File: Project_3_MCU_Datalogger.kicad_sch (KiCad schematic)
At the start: 25 parts, among them U1 24LC1025, U2 24LC1025, U3 DS1337S_, U4 ATMEGA328P-AU, Y1 16MHz, Y2 32.768 kHz

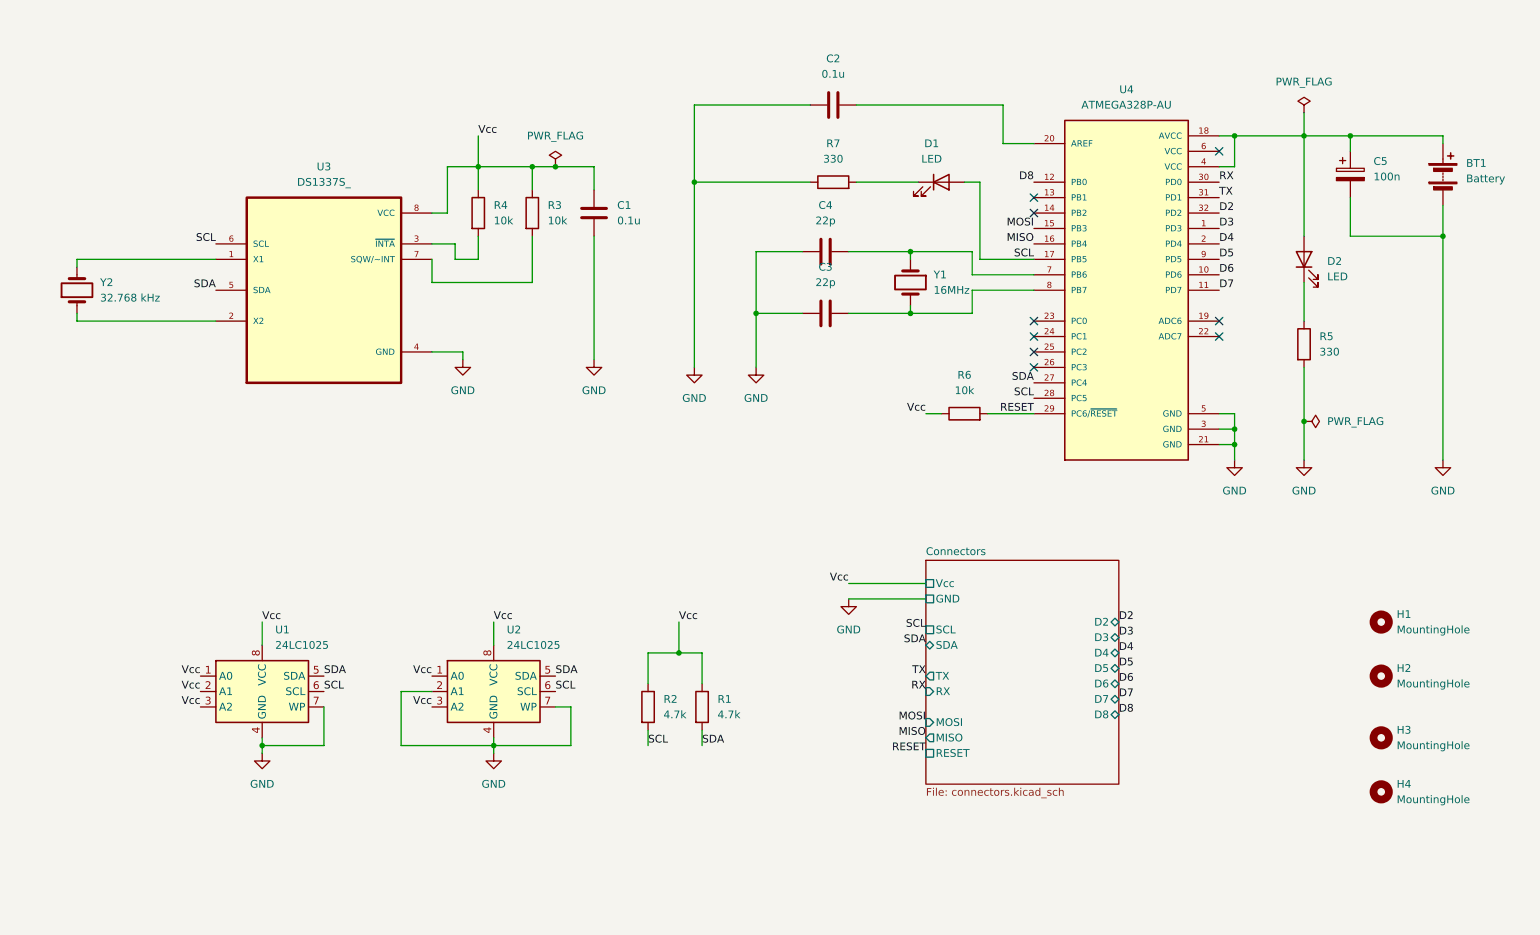
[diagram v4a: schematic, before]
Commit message: encadrement des blocs et présentation du circuit
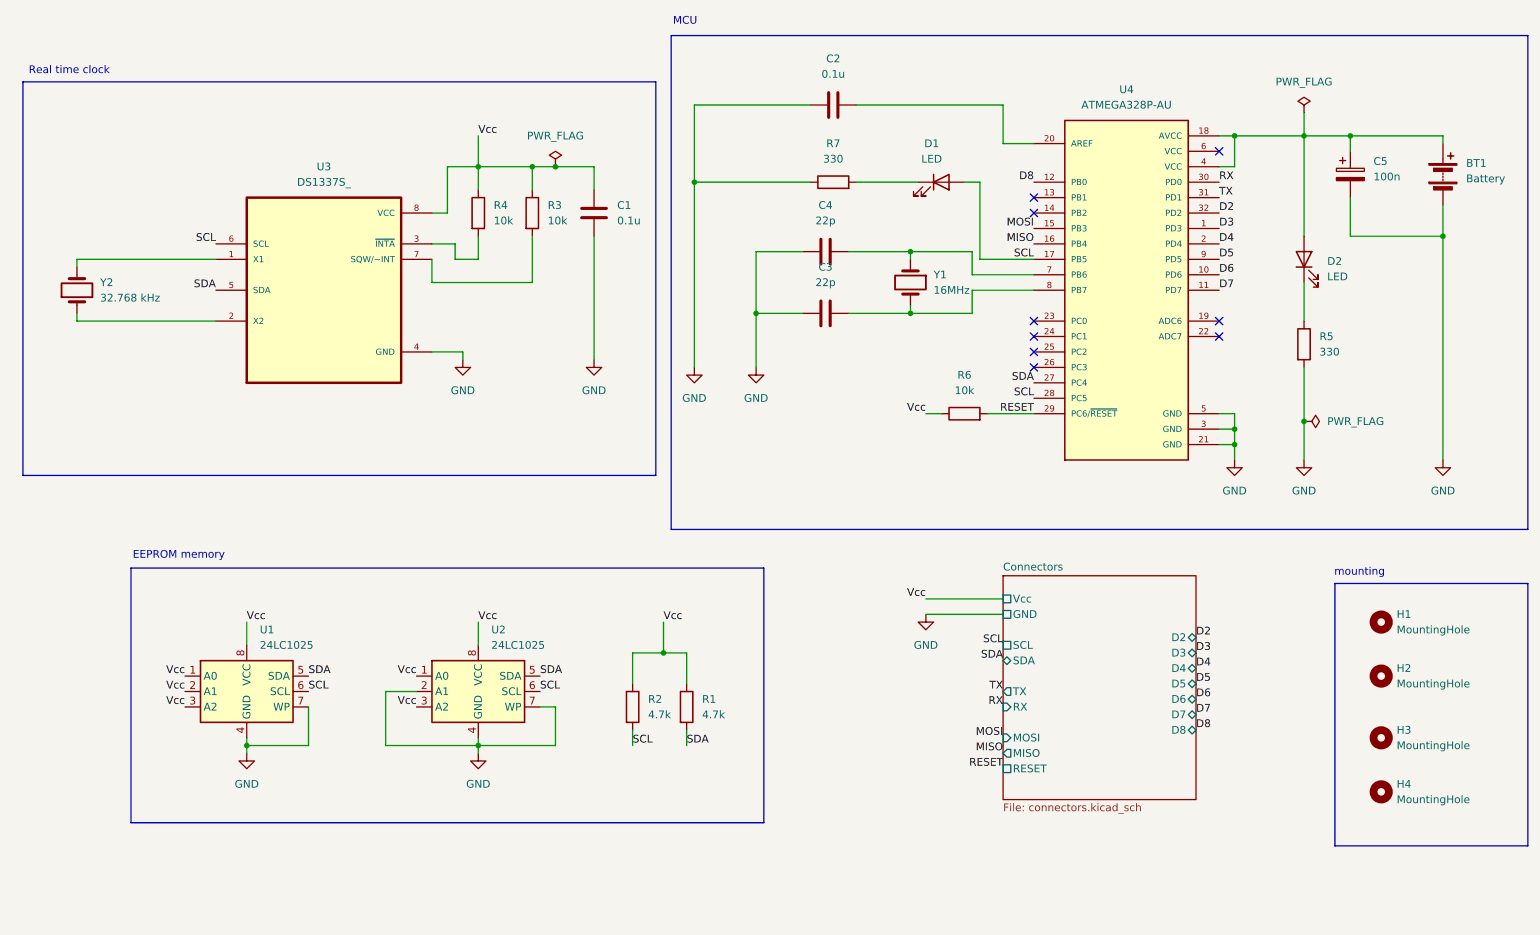
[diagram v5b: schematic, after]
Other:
- note added: "EEPROM memory"
- note added: "MCU"
- note added: "Real time clock"
- note added: "mounting"
- moved on the sheet: R1, R2, U1, U2

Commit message: amelioration disposition composants et changements circuit
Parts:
- removed C5: 100n, Capacitor_SMD:C_0805_2012Metric, symbol Device:C_Polarized
- added C5: 100n, Capacitor_SMD:C_0805_2012Metric, symbol Device:C
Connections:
- net GND: now also C5.2
- net SCL: no longer D1.2 (A), U4.17 (PB5)
- net Vcc: now also BT1.1 (+), D2.2 (A), U4.18 (AVCC), U4.4 (VCC), C5.1
- net at U4.13 (PB1): now also D1.2 (A)
- new net SCK: U4.17 (PB5)
- no-connect marks 9 -> 8
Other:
- note added: "Pull up resistor I2C bus"
- moved on the sheet: R1, R2

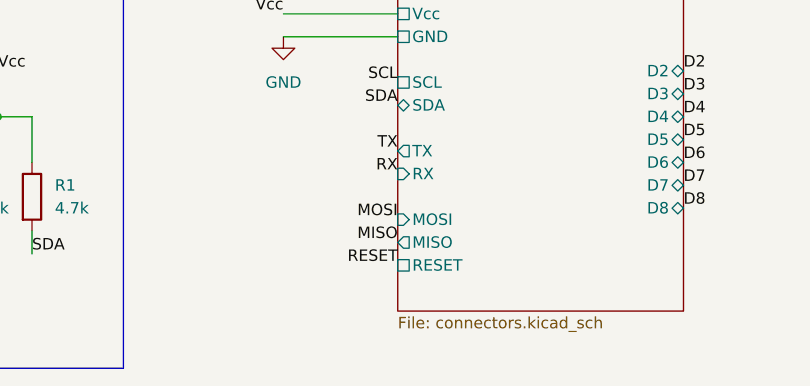
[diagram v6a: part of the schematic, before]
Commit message: Fin du routage sur deux couches et modifications du schema
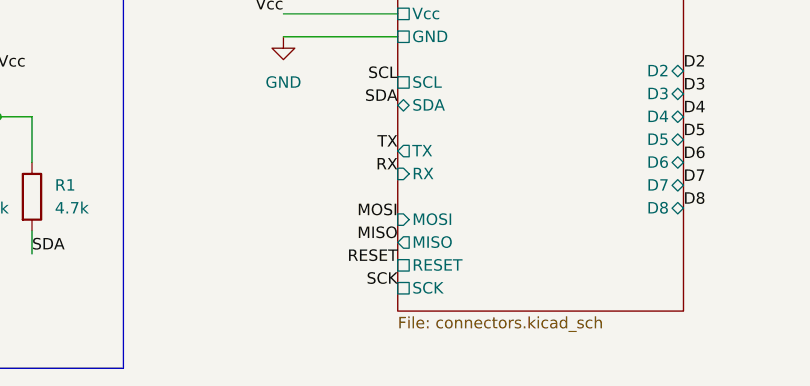
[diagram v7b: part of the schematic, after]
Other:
- sheet Connectors ports: added SCK; removed none
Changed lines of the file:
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@@
 		)
 	)
+	(label "SCK"
+		(at 191.77 151.13 180)
+		(effects
+			(font
+				(size 1.27 1.27)
+			)
+			(justify right bottom)
+		)
+	)
 	(label "Vcc"
 		(at 53.34 130.81 180)
@@
 			(effects
 				(font
+					(size 1.27 1.27)
+				)
+				(justify left)
+			)
+		)
+		(pin "SCK" passive
+			(at 191.77 151.13 180)
+			(effects
+				(font
